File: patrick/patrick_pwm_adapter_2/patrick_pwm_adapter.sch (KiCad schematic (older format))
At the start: 10 parts, among them IC1 IS32FL3237-TQLA3, J1 Conn_01x13, J2 Conn_01x13

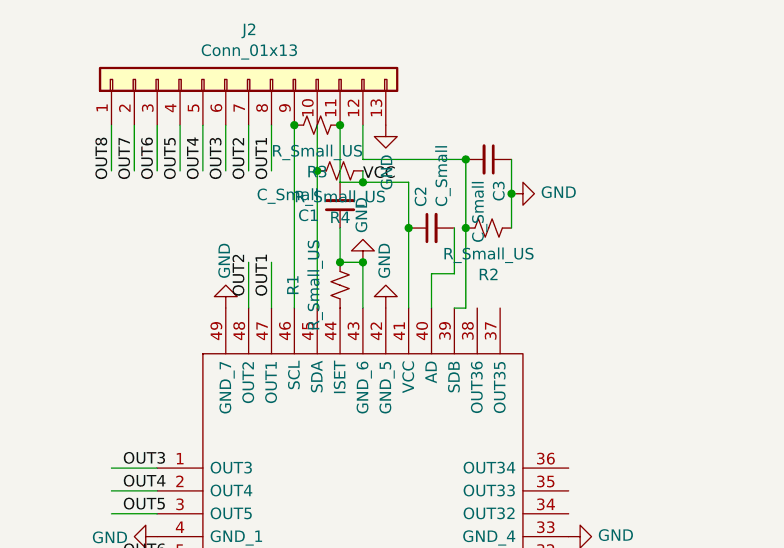
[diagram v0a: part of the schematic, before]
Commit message: slight change to correct problem with IS32 breakout board
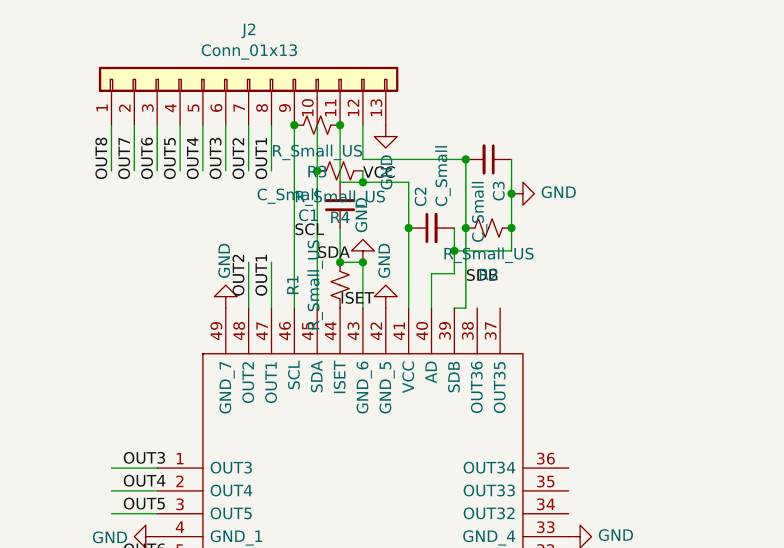
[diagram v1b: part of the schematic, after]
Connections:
- net labels added: ISET, SCL, SDA, SDB
- wire segments 62 -> 65
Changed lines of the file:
@@
 	7700 1700 7800 1700
-Wire Wire Line
-	7800 1700 7800 1500
 Wire Wire Line
 	7300 1300 7400 1300
@@
 Wire Wire Line
 	8050 1200 8050 1350
+Text Label 7100 1550 0    50   ~ 0
+SCL
+Text Label 7200 1650 0    50   ~ 0
+SDA
+Wire Wire Line
+	7800 1600 8050 1600
+Wire Wire Line
+	8050 1600 8050 1500
+Wire Wire Line
+	7800 1500 7800 1600
+Connection ~ 7800 1600
+Wire Wire Line
+	7800 1600 7800 1700
+Connection ~ 8050 1500
+Text Label 7850 1750 0    50   ~ 0
+SDB
+Text Label 7300 1850 0    50   ~ 0
+ISET
 $EndSCHEMATC
